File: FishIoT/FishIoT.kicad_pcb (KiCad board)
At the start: 4 copper layers, 42 x 70 mm, 117 parts, among them IC1 RV-3032-C7_32.768KHZ-2.5PPM-T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, J1 USB4105-GF-A-120, J3 Conn_Coaxial, J4 BM05B-ZESS-TBT, J5 SF72S006VBDR2500, J6 Conn_Coaxial, J7 SHF-105-01-L-D-SM, J8 0705430001, SW1 PTS645SM43SMTR92 LF, SW2 PTS645SM43SMTR92 LF, SW3 PTS645SM43SMTR92 LF, U1 USBLC6-2P6, U2 NRF9151-LACA-R7, U3 CP2102N-Axx-xQFN20, U4 MAX-M10S, U5 TPD3F303DPVR, U6 MAX3471, U7 SI1040X-T1-GE3, U8 TPS63000

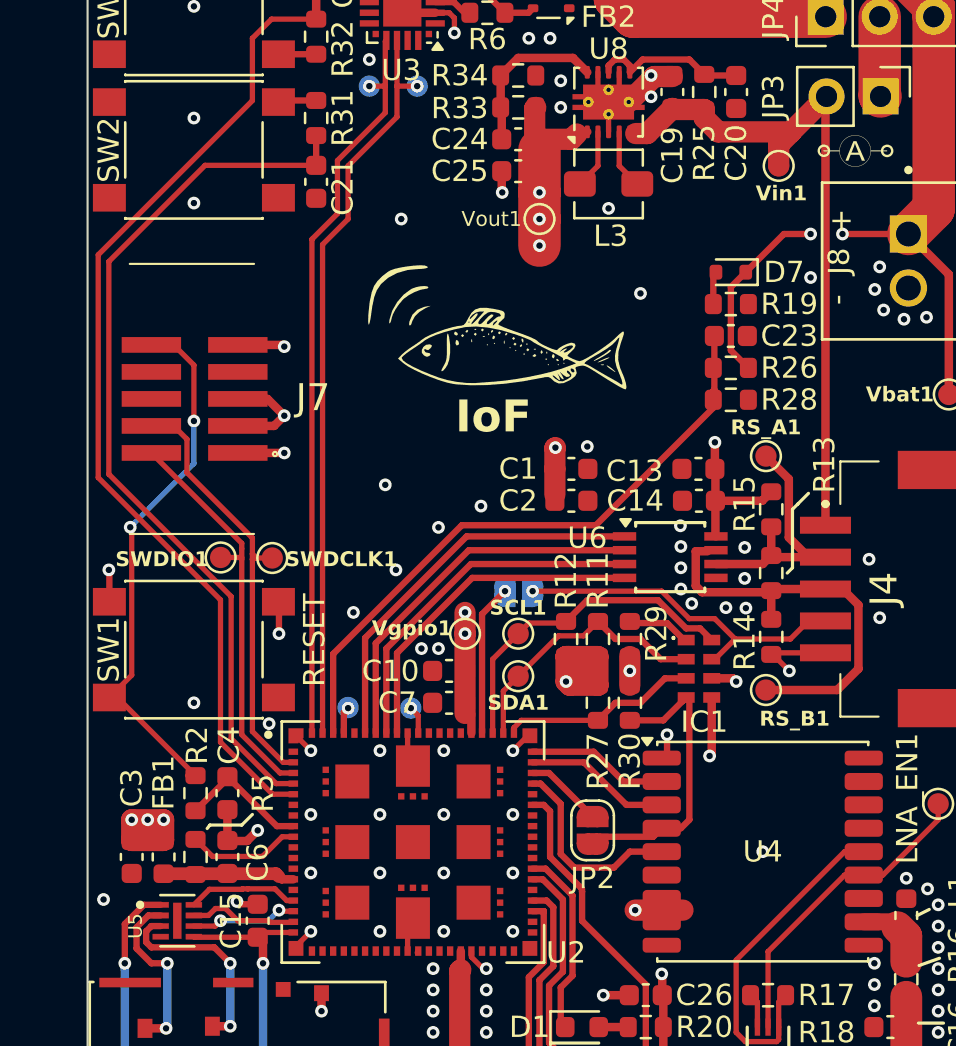
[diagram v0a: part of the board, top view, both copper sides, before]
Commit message: Added LoRa module
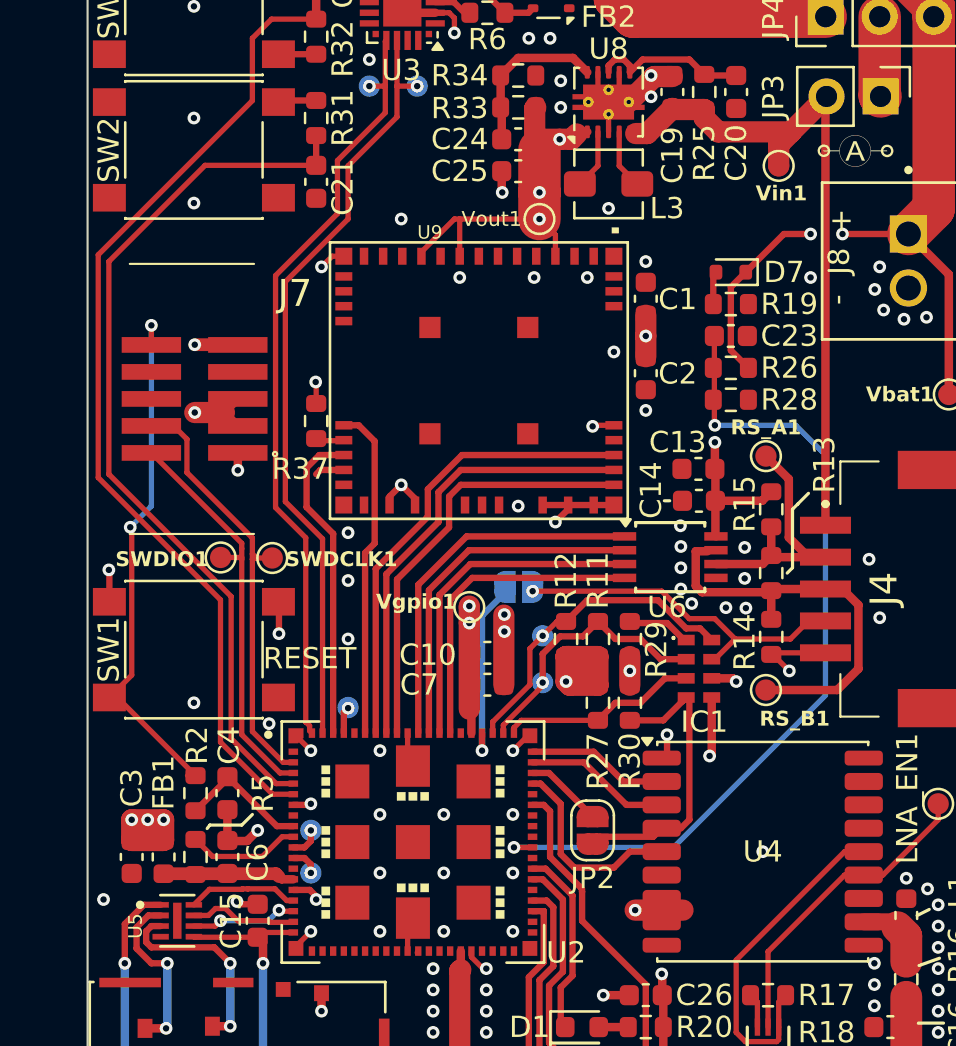
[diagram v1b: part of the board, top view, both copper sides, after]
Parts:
- removed GPIO_0.11: TestPoint, TestPoint:TestPoint_Pad_D1.0mm
- added GPIO_P.024: TestPoint, TestPoint:TestPoint_Pad_D1.0mm, B.Cu at (103.0, 80.2)
- added GPIO_P.025: TestPoint, TestPoint:TestPoint_Pad_D1.0mm, B.Cu at (103.0, 82.2)
- added R37: 10k, Resistor_SMD:R_0603_1608Metric, F.Cu at (103.2, 61.0)
- added U9: RM126x, FishIoT_Footprint_library:Laird, RM126X, F.Cu at (110.9, 59.1)
- G***, SCL1, SDA1: moved to B.Cu
- moved G*** 13.6 mm to (122.0, 48.0), turned to -90 degrees
- moved C1 8.73 mm to (118.8, 55.2), turned to -90 degrees
- moved C2 6.95 mm to (118.8, 58.8), turned to 90 degrees
- moved C10 1.99 mm to (111.3, 71.9), turned to 0 degrees
- moved C7 1.99 mm to (111.3, 73.4), turned to 0 degrees
- moved Vgpio1 1.27 mm to (110.5, 69.8)
- moved SDA1 1.19 mm to (113.9, 73.3), turned to 180 degrees
- moved SCL1 1.15 mm to (113.9, 71.1), turned to 180 degrees
- moved JP1 0.20 mm to (112.8, 68.8)
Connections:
- U2 pad 11: unconnected-(U2A-P0.24/TRACEDATA(2)-Pad11) -> Net-(U2A-P0.24/TRACEDATA(2))
- U2 pad 12: unconnected-(U2A-P0.25/TRACEDATA(3)-Pad12) -> Net-(U2A-P0.25/TRACEDATA(3))
- U2 pad 50: unconnected-(U2A-P0.31-Pad50) -> /Battery_voltage
- U2 pad 67: unconnected-(U2A-P0.08-Pad67) -> /RS485_DI
- U2 pad 68: unconnected-(U2A-P0.09-Pad68) -> /RS485_DE
- U2 pad 69: unconnected-(U2A-P0.10-Pad69) -> /RS485_RE
- U2 pad 70: Net-(U2A-P0.11) -> /RS485_RX
- U2 pad 72: /RS485_DI -> /RM_CTS
- U2 pad 73: /RS485_DE -> /RM_RX
- U2 pad 74: /RS485_RE -> /RM_RTS
- U2 pad 75: /RS485_RX -> /RM_TX
- U2 pad 78: /Battery_voltage -> /RM_RESETn
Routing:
- net /RM_RTS: track 0.00 -> 21.9 mm
- net /RM_RX: track 0.00 -> 21.0 mm
- net /RM_CTS: track 0.00 -> 20.1 mm
- net /RM_TX: track 0.00 -> 15.7 mm
- net /RM_RESETn: track 0.00 -> 15.0 mm
- net GND: track 72.8 -> 87.3 mm, vias 133 -> 138
- net /Battery_voltage: track 29.8 -> 39.9 mm, vias 0 -> 2
- net +3V3: track 50.9 -> 60.3 mm, vias 15 -> 17
- net Net-(JP1-A): track 7.12 -> 8.82 mm
- net /VUSB_C: track 14.1 -> 15.6 mm
- net /nRF_UART_RX: track 35.0 -> 36.4 mm
- net Net-(U2A-P0.24/TRACEDATA(2)): track 0.00 -> 1.45 mm, vias 0 -> 1
- net /nRF_UART_TX: track 34.8 -> 36.2 mm
- net Net-(U2A-P0.25/TRACEDATA(3)): track 0.00 -> 1.35 mm, vias 0 -> 1
- net Net-(U2A-P0.11): track 1.32 -> 0.00 mm, vias 1 -> 0
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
